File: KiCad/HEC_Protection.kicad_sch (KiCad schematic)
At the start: 17 parts, among them U11 74LS00, U11 74LS32, U12 74LS04, U17 74LS74, U18 74LS138, U18 74LS74, U19 74LS30, U22 74LS02, U24 74LS74, U25 74LS541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

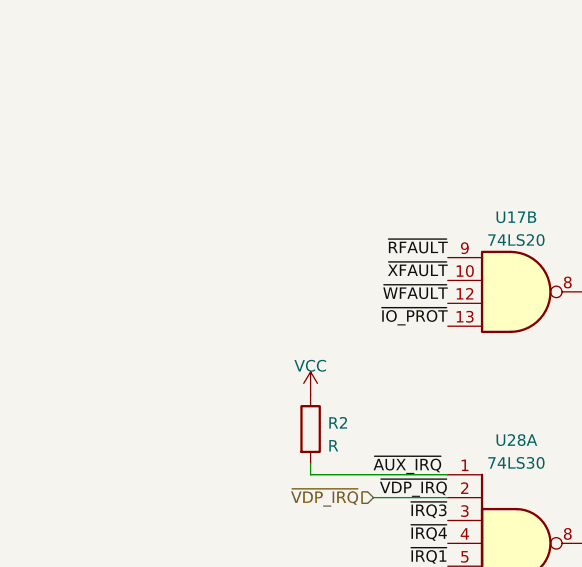
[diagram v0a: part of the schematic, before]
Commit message: Preliminary layout
Very early stage layout prototype, very subject to change.
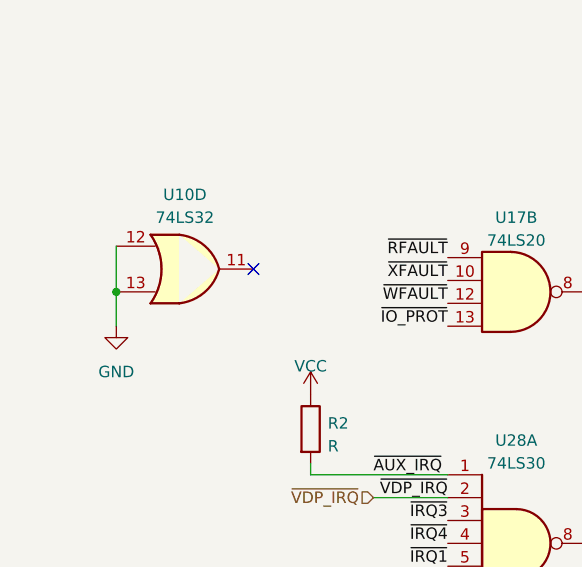
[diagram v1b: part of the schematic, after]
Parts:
- added U10: 74LS32, Package_DIP:DIP-14_W7.62mm_Socket, symbol 74xx:74LS32
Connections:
- net GND: now also U10.12, U10.13
- no-connect marks 13 -> 14
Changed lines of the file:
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@@
   (junction (at 234.315 45.085) (diameter 0) (color 0 0 0 0)
+  )
+  (junction (at 24.765 38.735) (diameter 0) (color 0 0 0 0)
   )
   (junction (at 121.285 139.065) (diameter 0) (color 0 0 0 0)
@@
   (no_connect (at 199.39 53.34))
   (no_connect (at 166.37 140.97))
+  (no_connect (at 40.005 36.195))
   (no_connect (at 262.89 90.17))
   (no_connect (at 165.735 96.52))
@@
     (stroke (width 0) (type default))
   )
+  (wire (pts (xy 24.765 33.655) (xy 24.765 38.735))
+    (stroke (width 0) (type default))
+  )
   (wire (pts (xy 31.115 85.09) (xy 43.815 85.09))
     (stroke (width 0) (type default))
   )
   (wire (pts (xy 144.145 93.98) (xy 150.495 93.98))
+    (stroke (width 0) (type default))
+  )
+  (wire (pts (xy 24.765 38.735) (xy 24.765 42.545))
     (stroke (width 0) (type default))
   )
@@
         (path "/87935374-b60a-4f41-99da-94b76103dd77/2930b625-d6a3-4a7f-9d41-a454efcef99d"
           (reference "#PWR037") (unit 1)
+        )
+      )
+    )
+  )
+  (symbol (lib_id "74xx:74LS32") (at 32.385 36.195 0) (unit 4)
+    (in_bom yes) (on_board yes) (dnp no) (fields_autoplaced)
+    (property "Reference" "U10" (at 32.385 27.94 0)
+      (effects (font (size 1.27 1.27)))
+    )
+    (property "Value" "74LS32" (at 32.385 30.48 0)
+      (effects (font (size 1.27 1.27)))
+    )
+    (property "Footprint" "Package_DIP:DIP-14_W7.62mm_Socket" (at 32.385 36.195 0)
+      (effects (font (size 1.27 1.27)) hide)
+    )
+    (property "Datasheet" "http://www.ti.com/lit/gpn/sn74LS32" (at 32.385 36.195 0)
+      (effects (font (size 1.27 1.27)) hide)
+    )
+    (pin "1")
+    (pin "2")
+    (pin "3")
+    (pin "4")
+    (pin "5")
+    (pin "6")
+    (pin "10")
+    (pin "8")
+    (pin "9")
+    (pin "11")
+    (pin "12")
+    (pin "13")
+    (pin "14")
+    (pin "7")
+    (instances
+      (project "HEC1"
+        (path "/87935374-b60a-4f41-99da-94b76103dd77/933a6f90-eb98-4eb1-8c19-8a76228aece1"
+          (reference "U10") (unit 4)
+        )
+        (path "/87935374-b60a-4f41-99da-94b76103dd77/2930b625-d6a3-4a7f-9d41-a454efcef99d"
+          (reference "U10") (unit 4)
         )
       )
@@
         )
       )
+    )
+  )
+  (symbol (lib_id "power:GND") (at 24.765 42.545 0) (unit 1)
+    (in_bom yes) (on_board yes) (dnp no) (fields_autoplaced)
+    (property "Reference" "#PWR0108" (at 24.765 48.895 0)
+      (effects (font (size 1.27 1.27)) hide)
+    )
+    (property "Value" "GND" (at 24.765 47.625 0)
+      (effects (font (size 1.27 1.27)))
+    )
+    (property "Footprint" "" (at 24.765 42.545 0)
+      (effects (font (size 1.27 1.27)) hide)
+    )
+    (property "Datasheet" "" (at 24.765 42.545 0)
+      (effects (font (size 1.27 1.27)) hide)
+    )
+    (pin "1")
+    (instances
+      (project "HEC1"
+        (path "/87935374-b60a-4f41-99da-94b76103dd77"
+          (reference "#PWR0108") (unit 1)
+        )
+        (path "/87935374-b60a-4f41-99da-94b76103dd77/933a6f90-eb98-4eb1-8c19-8a76228aece1"
+          (reference "#PWR0109") (unit 1)
+        )
+        (path "/87935374-b60a-4f41-99da-94b76103dd77/2930b625-d6a3-4a7f-9d41-a454efcef99d"
+          (reference "#PWR0109") (unit 1)
+        )
+      )

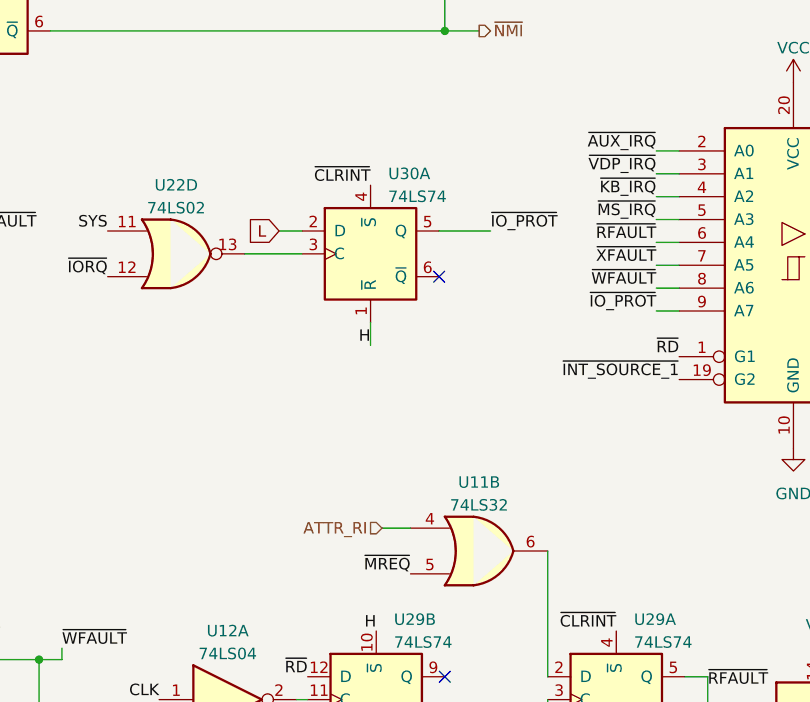
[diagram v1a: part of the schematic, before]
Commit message: Updated layout
Updated the layout of PCB. Chips on the board in this version might be in their final position.
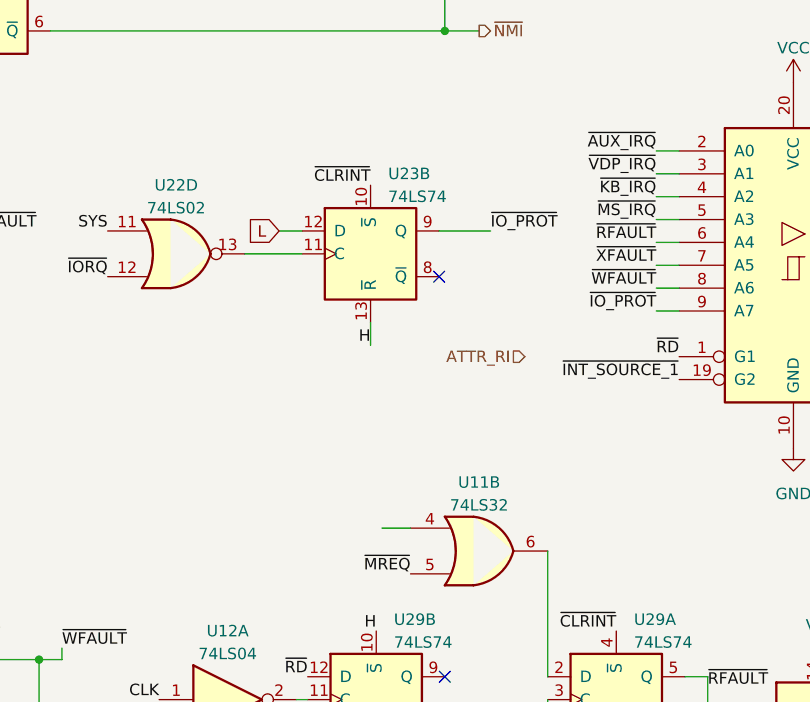
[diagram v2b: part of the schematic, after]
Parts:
- removed unit 1 of U30
- added U23: 74LS74, Package_DIP:DIP-14_W7.62mm_Socket, symbol 74xx:74LS74
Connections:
- net ATTR_RI: no longer U11.4
- net H: now also U23.13 (~{R})
- net L: now also U23.12 (D)
- net ~{CLRINT}: now also U23.10 (~{S})
- net ~{IO_PROT}: now also U23.9 (Q)
- net at U22.13: now also U23.11 (C)
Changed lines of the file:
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@@
     (effects (font (size 1.27 1.27)) (justify right))
   )
-  (hierarchical_label "ATTR_RI" (shape input) (at 159.385 124.46 180) (fields_autoplaced)
+  (hierarchical_label "ATTR_RI" (shape input) (at 175.26 105.41 180) (fields_autoplaced)
     (effects (font (size 1.27 1.27)) (justify right))
   )
@@
         (path "/87935374-b60a-4f41-99da-94b76103dd77/2930b625-d6a3-4a7f-9d41-a454efcef99d"
           (reference "U27") (unit 3)
+        )
+      )
+    )
+  )
+  (symbol (lib_id "74xx:74LS74") (at 158.115 93.98 0) (unit 2)
+    (in_bom yes) (on_board yes) (dnp no) (fields_autoplaced)
+    (property "Reference" "U23" (at 160.0709 85.09 0)
+      (effects (font (size 1.27 1.27)) (justify left))
+    )
+    (property "Value" "74LS74" (at 160.0709 87.63 0)
+      (effects (font (size 1.27 1.27)) (justify left))
+    )
+    (property "Footprint" "Package_DIP:DIP-14_W7.62mm_Socket" (at 158.115 93.98 0)
+      (effects (font (size 1.27 1.27)) hide)
+    )
+    (property "Datasheet" "74xx/74hc_hct74.pdf" (at 158.115 93.98 0)
+      (effects (font (size 1.27 1.27)) hide)
+    )
+    (pin "1")
+    (pin "2")
+    (pin "3")
+    (pin "4")
+    (pin "5")
+    (pin "6")
+    (pin "10")
+    (pin "11")
+    (pin "12")
+    (pin "13")
+    (pin "8")
+    (pin "9")
+    (pin "14")
+    (pin "7")
+    (instances
+      (project "HEC1"
+        (path "/87935374-b60a-4f41-99da-94b76103dd77/73a0c68b-1e42-4c0d-ae31-b1a96d0648bb"
+          (reference "U23") (unit 2)
+        )
+        (path "/87935374-b60a-4f41-99da-94b76103dd77/2930b625-d6a3-4a7f-9d41-a454efcef99d"
+          (reference "U23") (unit 2)
         )
       )
@@
         )
       )
-    )
-  )
-  (symbol (lib_id "74xx:74LS74") (at 158.115 93.98 0) (unit 1)
-    (in_bom yes) (on_board yes) (dnp no) (fields_autoplaced)
-    (property "Reference" "U30" (at 160.0709 85.09 0)
-      (effects (font (size 1.27 1.27)) (justify left))
-    )
-    (property "Value" "74LS74" (at 160.0709 87.63 0)
-      (effects (font (size 1.27 1.27)) (justify left))
-    )
-    (property "Footprint" "Package_DIP:DIP-14_W7.62mm_Socket" (at 158.115 93.98 0)
-      (effects (font (size 1.27 1.27)) hide)
-    )
-    (property "Datasheet" "74xx/74hc_hct74.pdf" (at 158.115 93.98 0)
-      (effects (font (size 1.27 1.27)) hide)
-    )
-    (pin "1")
-    (pin "2")
-    (pin "3")
-    (pin "4")
-    (pin "5")
-    (pin "6")
-    (pin "10")
-    (pin "11")
-    (pin "12")
-    (pin "13")
-    (pin "8")
-    (pin "9")
-    (pin "14")
-    (pin "7")
-    (instances
-      (project "HEC1"
-        (path "/87935374-b60a-4f41-99da-94b76103dd77/2930b625-d6a3-4a7f-9d41-a454efcef99d"
-          (reference "U30") (unit 1)
-        )
-      )
